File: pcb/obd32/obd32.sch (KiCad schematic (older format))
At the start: 36 parts, among them J1 USB_C_Receptacle_USB2.0, J2 Micro_SD_Card, J3 Conn_02x08_Top_Bottom, J4 USB_A, U1 LMR33630ADDA, U2 CP2102N-A01-GQFN24, U3 AP1117-33, U4 ESP32-WROOM-32, U5 SiP32431DR3, U6 MCP2562-E-MF

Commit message: Maybe version of board
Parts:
- removed C7, C8: 22µF, Capacitor_SMD:C_0805_2012Metric, symbol Device:C
- removed J1: USB_C_Receptacle_USB2.0, Connector_USB:USB_C_Receptacle_HRO_TYPE-C-31-M-12, symbol Connector:USB_C_Receptacle_USB2.0
- removed J3: Conn_02x08_Top_Bottom, Connector_PinHeader_2.54mm:PinHeader_2x08_P2.54mm_Vertical, symbol Connector_Generic:Conn_02x08_Top_Bottom
- removed J4: USB_A, Connector_USB:USB_A_Molex_105057_Vertical, symbol Connector:USB_A
- removed U1: LMR33630ADDA, Package_SO:Texas_HSOP-8-1EP_3.9x4.9mm_P1.27mm_ThermalVias, symbol Regulator_Switching:LMR33630ADDA
- removed U2: CP2102N-A01-GQFN24, Package_DFN_QFN:QFN-24-1EP_4x4mm_P0.5mm_EP2.6x2.6mm, symbol Interface_USB:CP2102N-A01-GQFN24
- added C15: 10nF, Capacitor_SMD:C_0201_0603Metric, symbol Device:C
- added C16: 0.47µF, Capacitor_SMD:C_0201_0603Metric, symbol Device:C
- added C17, C18: 0.1µF, Capacitor_SMD:C_0201_0603Metric, symbol Device:C
- added D3, D4, D5: LED, LED_SMD:LED_0402_1005Metric, symbol Device:LED
- added J1: Conn_01x04_Male, Connector_Molex:Molex_PicoBlade_53048-0410_1x04_P1.25mm_Horizontal, symbol Connector:Conn_01x04_Male
- added J3: OBD2, OBD2:OBD2, symbol OBD2:OBD2
- added J4: 67329-8040, 67329-8040:673298040, symbol 67329-8040:67329-8040
- added J5: Conn_01x04_Female, Connector_PinSocket_2.54mm:PinSocket_1x04_P2.54mm_Vertical_SMD_Pin1Left, symbol Connector:Conn_01x04_Female
- added R10, R11: 4K7, Resistor_SMD:R_0201_0603Metric, symbol Device:R
- added R12, R13: 65R, Resistor_SMD:R_0201_0603Metric, symbol Device:R
- added R14: 5R, Resistor_SMD:R_0201_0603Metric, symbol Device:R
- added SW1, SW2: SW_Push, Button_Switch_SMD:SW_SPST_B3U-3000P-B, symbol Switch:SW_Push
- added U1: LMR33630BDDA, Package_SO:Texas_HSOP-8-1EP_3.9x4.9mm_P1.27mm_ThermalVias, symbol Regulator_Switching:LMR33630BDDA
- added U2: ICM-20689, ICM-20689:QFN50P400X400X95-25N-D, symbol ICM-20689:ICM-20689
- added U7: LPS25HB, Package_LGA:ST_HLGA-10_2.5x2.5mm_P0.6mm_LayoutBorder3x2y, symbol Sensor_Pressure:LPS25HB
- C11, C12, C13, C14, C4: value 100nF -> 0.1µF; footprint Capacitor_SMD:C_0805_2012Metric -> Capacitor_SMD:C_0201_0603Metric
- C3: footprint Capacitor_SMD:C_0805_2012Metric -> Capacitor_SMD:C_0402_1005Metric
- C9: footprint Capacitor_SMD:C_0805_2012Metric -> Capacitor_SMD:C_0603_1608Metric
- L1: value 8µH -> 2.2µH; footprint Inductor_SMD:L_Coilcraft_XxL4040 -> TDK_SPM5030:TDK_SPM5030
- R1, R2, R3, R4, R7, R8, R9: footprint Resistor_SMD:R_0603_1608Metric -> Resistor_SMD:R_0201_0603Metric
- R5, R6: value 5K1 -> 100K; footprint Resistor_SMD:R_0603_1608Metric -> Resistor_SMD:R_0201_0603Metric
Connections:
- net labels added: BARO_INT, ESP32_EN, ESP32_MISC, GPS_RX, GPS_TX, I2C0_SCL, I2C0_SDA, IMU_INT, LED_B, LED_G, LED_R
- net labels removed: Earth, USB_D+, USB_D-
- wire segments 72 -> 75
- no-connect marks 0 -> 2
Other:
- moved on the sheet: C11, C12, R7, R8, U4, U5

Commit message: Board: Add USB-C and CP2102 UART converter
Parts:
- removed J1: Conn_01x04_Male, Connector_Molex:Molex_PicoBlade_53048-0410_1x04_P1.25mm_Horizontal, symbol Connector:Conn_01x04_Male
- added C7: 4.7µF, Capacitor_SMD:C_0201_0603Metric, symbol Device:C
- added C8: 0.1µF, Capacitor_SMD:C_0201_0603Metric, symbol Device:C
- added D6: SP0503BAHT, Package_TO_SOT_SMD:SOT-143, symbol Power_Protection:SP0503BAHT
- added J1: USB_C_Receptacle_USB2.0, Connector_USB:USB_C_Receptacle_HRO_TYPE-C-31-M-12, symbol Connector:USB_C_Receptacle_USB2.0
- added R15: 1K, Resistor_SMD:R_0201_0603Metric, symbol Device:R
- added R16, R17: 5.1K, Resistor_SMD:R_0201_0603Metric, symbol Device:R
- added U8: CP2102N-A01-GQFN24, Package_DFN_QFN:QFN-24-1EP_4x4mm_P0.5mm_EP2.6x2.6mm, symbol Interface_USB:CP2102N-A01-GQFN24
- C4: footprint Capacitor_SMD:C_0201_0603Metric -> Capacitor_SMD:C_0402_1005Metric
- C9: footprint Capacitor_SMD:C_0603_1608Metric -> Capacitor_SMD:C_0805_2012Metric
- U3: value AP1117-33 -> AZ1117C-3.3; footprint Package_TO_SOT_SMD:SOT-223-3_TabPin2 -> Package_TO_SOT_SMD:SOT-89-3; symbol Regulator_Linear:AP1117-33 -> Regulator_Linear:AZ1117-3.3
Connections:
- net +3V3: now also C7.1, C8.1, R15.1, U8.5 (VIO), U8.6 (VDD)
- net +5VA: now also D6.2 (K), J1.A4 (VBUS), J1.A9 (VBUS), J1.B4 (VBUS), J1.B9 (VBUS)
- net GND: now also C7.2, C8.2, D6.1 (A), J1.A1 (GND), J1.A12 (GND), J1.B1 (GND), J1.B12 (GND), J1.S1 (SHIELD), R16.1, R17.2, U8.2 (GND), U8.25 (GND)
- net UART_RX: now also U8.21 (TXD)
- net UART_TX: now also U8.20 (RXD)
- new net: J1.A5 (CC1), R16.2
- new net: J1.B5 (CC2), R17.1
- new net: R15.2, U8.9 (~RSTb)
- new net USB_D+: D6.4 (K), J1.A6 (D+), J1.B6 (D+), U8.3 (D+)
- new net USB_D-: D6.3 (K), J1.A7 (D-), J1.B7 (D-), U8.4 (D-)
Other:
- moved on the sheet: C1, C10, C2, C3, C4, C5, C6, C9, D1, D2, J4, J5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

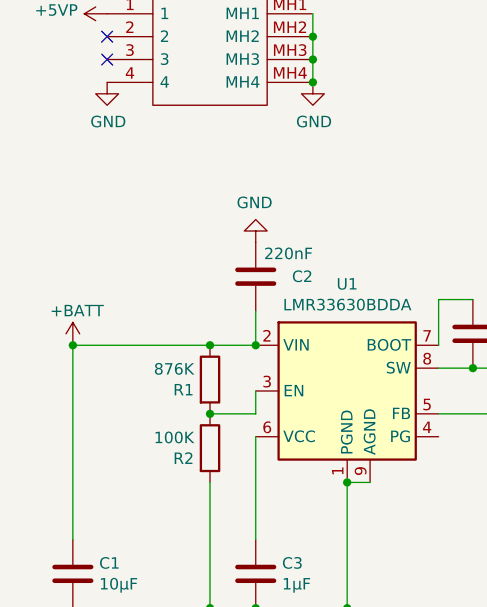
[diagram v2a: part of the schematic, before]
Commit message: Board: Add cuttable solder jumper to allow disconnection from 12V rail
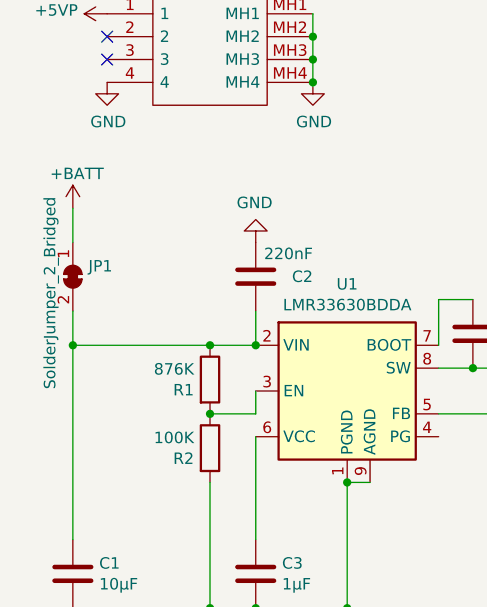
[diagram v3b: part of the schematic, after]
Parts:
- added JP1: SolderJumper_2_Bridged, Jumper:SolderJumper-2_P1.3mm_Bridged_RoundedPad1.0x1.5mm, symbol Jumper:SolderJumper_2_Bridged
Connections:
- net +BATT: now also JP1.1 (A); no longer C1.1, C2.2, R1.1, U1.2 (VIN)
- new net: C1.1, C2.2, JP1.2 (B), R1.1, U1.2 (VIN)
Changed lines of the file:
@@
 L power:+BATT #PWR0124
 U 1 1 5FC7D71E
-P 650 6400
-F 0 "#PWR0124" H 650 6250 50  0001 C CNN
-F 1 "+BATT" H 550 6550 50  0000 L CNN
-F 2 "" H 650 6400 50  0001 C CNN
-F 3 "" H 650 6400 50  0001 C CNN
-	1    650  6400
+P 650 5800
+F 0 "#PWR0124" H 650 5650 50  0001 C CNN
+F 1 "+BATT" H 550 5950 50  0000 L CNN
+F 2 "" H 650 5800 50  0001 C CNN
+F 3 "" H 650 5800 50  0001 C CNN
+	1    650  5800
 	1    0    0    -1
 $EndComp
@@
 Wire Wire Line
 	1850 7000 1950 7000
-Connection ~ 650  6400
 Wire Wire Line
 	650  6400 650  7250
@@
 	4800 6050 4900 6050
 Connection ~ 4900 6050
+$Comp
+L Jumper:SolderJumper_2_Bridged JP1
+U 1 1 5FC8024A
+P 650 6100
+F 0 "JP1" V 604 6168 50  0000 L CNN
+F 1 "SolderJumper_2_Bridged" H 300 6000 50  0000 L CNN
+F 2 "Jumper:SolderJumper-2_P1.3mm_Bridged_RoundedPad1.0x1.5mm" H 650 6100 50  0001 C CNN
+F 3 "~" H 650 6100 50  0001 C CNN
+	1    650  6100
+	0    1    1    0
+$EndComp
+Wire Wire Line
+	650  6250 650  6400
+Connection ~ 650  6400
+Wire Wire Line
+	650  5800 650  5950
 $EndSCHEMATC

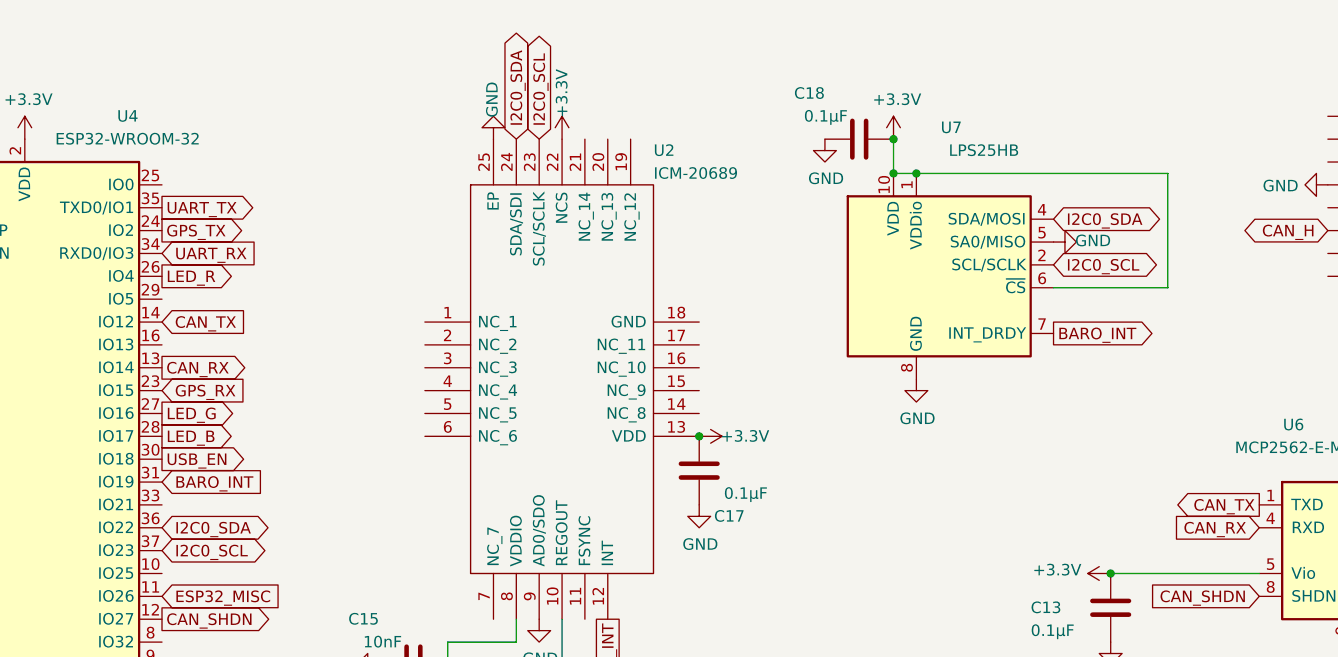
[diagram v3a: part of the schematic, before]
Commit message: Board: replace pressure sensor with more common bmp280
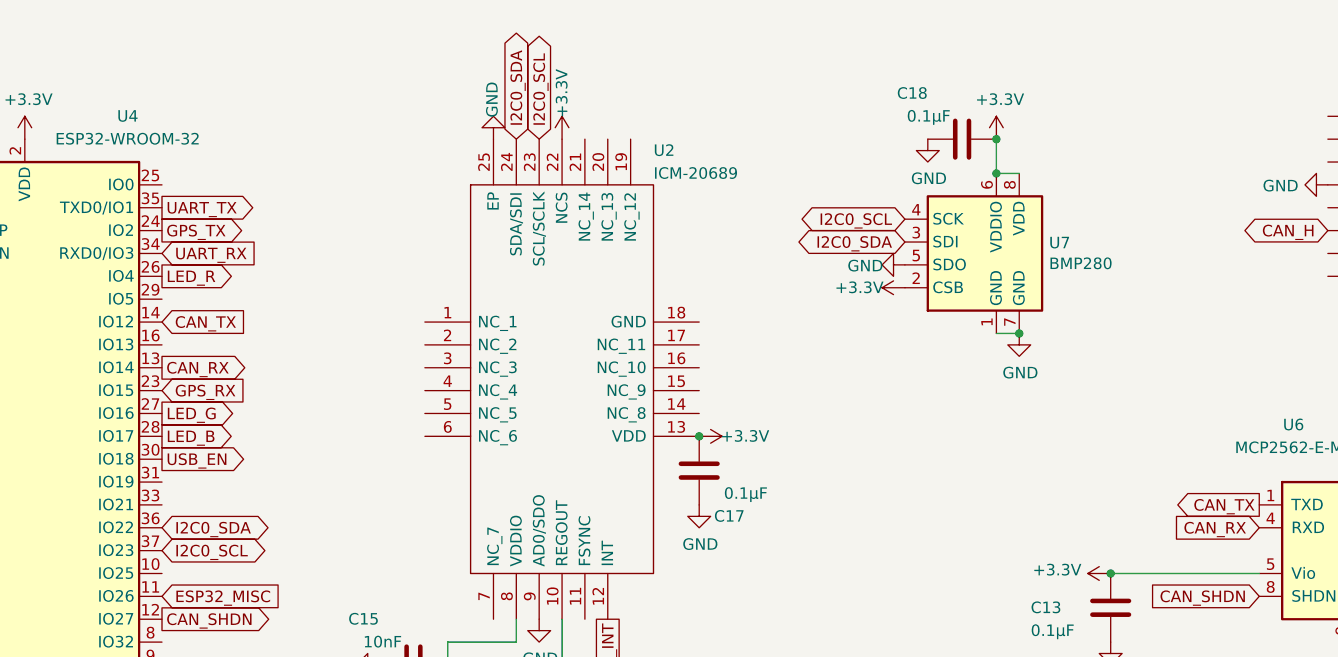
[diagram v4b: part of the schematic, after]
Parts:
- removed U7: LPS25HB, Package_LGA:ST_HLGA-10_2.5x2.5mm_P0.6mm_LayoutBorder3x2y, symbol Sensor_Pressure:LPS25HB
- added U7: BMP280, Package_LGA:Bosch_LGA-8_2x2.5mm_P0.65mm_ClockwisePinNumbering, symbol Sensor_Pressure:BMP280
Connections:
- net +3V3: now also U7.2 (CSB), U7.6 (VDDIO), U7.8 (VDD)
- net GND: now also U7.1 (GND), U7.5 (SDO), U7.7 (GND)
- net I2C0_SCL: now also U7.4 (SCK)
- net I2C0_SDA: now also U7.3 (SDI)
- net BARO_INT: no longer names the net of U4.31 (IO19)
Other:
- moved on the sheet: C18
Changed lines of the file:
@@
 	9650 6050 9650 6150
-$Comp
-L Sensor_Pressure:LPS25HB U7
-U 1 1 5FC7D0E2
-P 8050 1500
-F 0 "U7" H 8150 2100 50  0000 R CNN
-F 1 "LPS25HB" H 8400 2000 50  0000 R CNN
-F 2 "Package_LGA:ST_HLGA-10_2.5x2.5mm_P0.6mm_LayoutBorder3x2y" H 8050 1300 50  0001 C CNN
-F 3 "www.st.com/resource/en/datasheet/lps25hb.pdf" H 8100 1150 50  0001 C CNN
-	1    8050 1500
-	1    0    0    -1
-$EndComp
-Wire Wire Line
-	7950 1100 9050 1100
-Wire Wire Line
-	9050 1100 9050 1600
-Wire Wire Line
-	9050 1600 8550 1600
-$Comp
-L power:+3.3V #PWR0135
-U 1 1 5FC83F56
-P 7850 950
-F 0 "#PWR0135" H 7850 800 50  0001 C CNN
-F 1 "+3.3V" H 7865 1123 50  0000 C CNN
-F 2 "" H 7850 950 50  0001 C CNN
-F 3 "" H 7850 950 50  0001 C CNN
-	1    7850 950
-	1    0    0    -1
-$EndComp
 $Comp
 L power:+3.3V #PWR0136
@@
 L power:GND #PWR0137
 U 1 1 5FC84E03
-P 7950 2000
-F 0 "#PWR0137" H 7950 1750 50  0001 C CNN
-F 1 "GND" H 7955 1827 50  0000 C CNN
-F 2 "" H 7950 2000 50  0001 C CNN
-F 3 "" H 7950 2000 50  0001 C CNN
-	1    7950 2000
+P 8400 1800
+F 0 "#PWR0137" H 8400 1550 50  0001 C CNN
+F 1 "GND" H 8405 1627 50  0000 C CNN
+F 2 "" H 8400 1800 50  0001 C CNN
+F 3 "" H 8400 1800 50  0001 C CNN
+	1    8400 1800
 	1    0    0    -1
 $EndComp
@@
 Text GLabel 4650 2750 2    50   BiDi ~ 0
 I2C0_SCL
-Text GLabel 8550 1300 2    50   BiDi ~ 0
+Text GLabel 7900 1400 0    50   BiDi ~ 0
 I2C0_SDA
-Text GLabel 8550 1500 2    50   BiDi ~ 0
+Text GLabel 7900 1300 0    50   BiDi ~ 0
 I2C0_SCL
 Text GLabel 4650 3450 2    50   Input ~ 0
@@
 $EndComp
 Wire Wire Line
-	7950 1100 7850 1100
-Connection ~ 7950 1100
-Connection ~ 7850 1100
-$Comp
-L Device:C C18
-U 1 1 5FCF3A0C
-P 7700 950
-F 0 "C18" V 7900 1100 50  0000 L CNN
-F 1 "0.1µF" V 7800 1000 50  0000 L CNN
-F 2 "Capacitor_SMD:C_0201_0603Metric" H 7738 800 50  0001 C CNN
-F 3 "~" H 7700 950 50  0001 C CNN
-	1    7700 950
-	0    -1   -1   0
-$EndComp
-Wire Wire Line
-	7850 1100 7850 950
-Connection ~ 7850 950
-$Comp
-L power:GND #PWR0146
-U 1 1 5FCF66CC
-P 7550 950
-F 0 "#PWR0146" H 7550 700 50  0001 C CNN
-F 1 "GND" H 7555 777 50  0000 C CNN
-F 2 "" H 7550 950 50  0001 C CNN
-F 3 "" H 7550 950 50  0001 C CNN
-	1    7550 950
-	1    0    0    -1
-$EndComp
+	8400 1100 8300 1100
 $Comp
 L power:GND #PWR0147
 U 1 1 5FCF7087
-P 8550 1400
-F 0 "#PWR0147" H 8550 1150 50  0001 C CNN
-F 1 "GND" V 8555 1227 50  0000 C CNN
-F 2 "" H 8550 1400 50  0001 C CNN
-F 3 "" H 8550 1400 50  0001 C CNN
-	1    8550 1400
-	0    -1   -1   0
-$EndComp
-Text GLabel 8550 1800 2    50   Output ~ 0
-BARO_INT
-Text GLabel 4650 2450 2    50   Input ~ 0
-BARO_INT
+P 7900 1500
+F 0 "#PWR0147" H 7900 1250 50  0001 C CNN
+F 1 "GND" V 7905 1327 50  0000 C CNN
+F 2 "" H 7900 1500 50  0001 C CNN
+F 3 "" H 7900 1500 50  0001 C CNN
+	1    7900 1500
+	0    1    1    0
+$EndComp
 $Comp
 L OBD2:OBD2 J3
@@
 Wire Wire Line
 	650  5800 650  5950
+$Comp
+L Sensor_Pressure:BMP280 U7
+U 1 1 5FC9765F
+P 8300 1500
+F 0 "U7" H 8530 1596 50  0000 L CNN
+F 1 "BMP280" H 8530 1505 50  0000 L CNN
+F 2 "Package_LGA:Bosch_LGA-8_2x2.5mm_P0.65mm_ClockwisePinNumbering" H 8300 800 50  0001 C CNN
+F 3 "https://ae-bst.resource.bosch.com/media/_tech/media/datasheets/BST-BMP280-DS001.pdf" H 8300 1500 50  0001 C CNN
+	1    8300 1500
+	1    0    0    -1
+$EndComp
+Wire Wire Line
+	8300 1800 8400 1800
+Connection ~ 8400 1800
+Connection ~ 8300 1100
+$Comp
+L power:GND #PWR0146
+U 1 1 5FCF66CC
+P 8000 950
+F 0 "#PWR0146" H 8000 700 50  0001 C CNN
+F 1 "GND" H 8005 777 50  0000 C CNN
+F 2 "" H 8000 950 50  0001 C CNN
+F 3 "" H 8000 950 50  0001 C CNN
+	1    8000 950
+	1    0    0    -1
+$EndComp
+Connection ~ 8300 950
+Wire Wire Line
+	8300 1100 8300 950
+$Comp
+L Device:C C18
+U 1 1 5FCF3A0C
+P 8150 950
+F 0 "C18" V 8350 1100 50  0000 L CNN
+F 1 "0.1µF" V 8250 1000 50  0000 L CNN
+F 2 "Capacitor_SMD:C_0201_0603Metric" H 8188 800 50  0001 C CNN
+F 3 "~" H 8150 950 50  0001 C CNN
+	1    8150 950
+	0    -1   -1   0
+$EndComp
+$Comp
+L power:+3.3V #PWR0135
+U 1 1 5FC83F56
+P 8300 950
+F 0 "#PWR0135" H 8300 800 50  0001 C CNN
+F 1 "+3.3V" H 8315 1123 50  0000 C CNN
+F 2 "" H 8300 950 50  0001 C CNN
+F 3 "" H 8300 950 50  0001 C CNN
+	1    8300 950
+	1    0    0    -1
+$EndComp
+$Comp
+L power:+3.3V #PWR0159
+U 1 1 5FCB11BC
+P 7900 1600
+F 0 "#PWR0159" H 7900 1450 50  0001 C CNN
+F 1 "+3.3V" V 7900 1800 50  0000 C CNN
+F 2 "" H 7900 1600 50  0001 C CNN
+F 3 "" H 7900 1600 50  0001 C CNN
+	1    7900 1600
+	0    -1   -1   0
+$EndComp
 $EndSCHEMATC

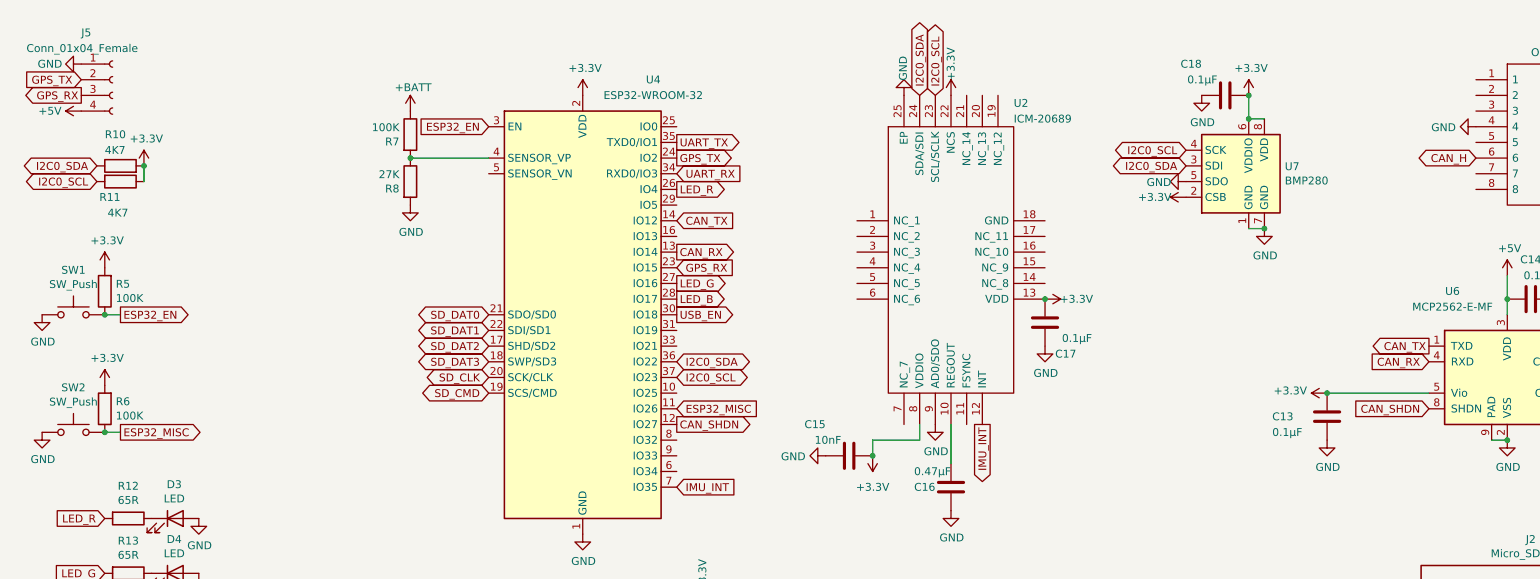
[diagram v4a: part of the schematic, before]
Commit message: Board: some refinement; Add button BOOT0
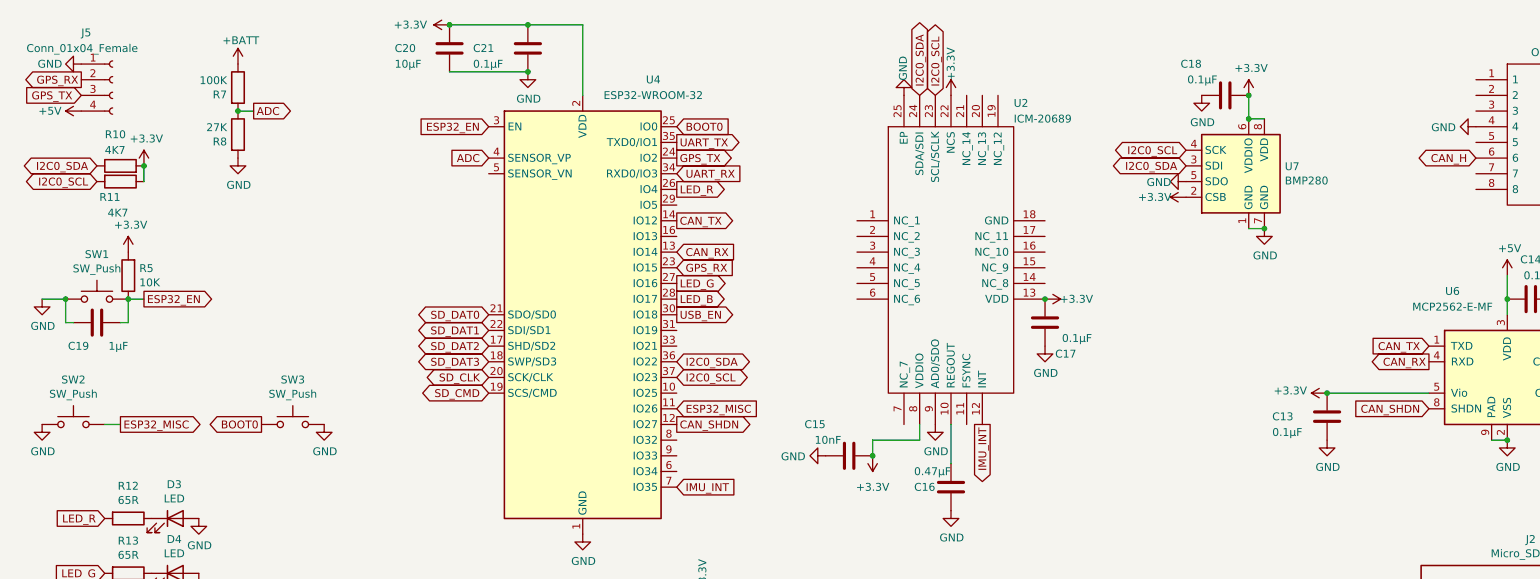
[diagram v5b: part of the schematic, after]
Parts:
- removed R6: 100K, Resistor_SMD:R_0201_0603Metric, symbol Device:R
- added C19: 1µF, Capacitor_SMD:C_0201_0603Metric, symbol Device:C
- added C20: 10µF, Capacitor_SMD:C_0805_2012Metric, symbol Device:C
- added C21: 0.1µF, Capacitor_SMD:C_0201_0603Metric, symbol Device:C
- added SW3: SW_Push, Button_Switch_SMD:SW_SPST_B3U-3000P-B, symbol Switch:SW_Push
- R5: value 100K -> 10K
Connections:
- net +3V3: now also C20.1, C21.1
- net ESP32_EN: now also C19.2
- net GND: now also C19.1, C20.2, C21.2, SW3.2
- net GPS_RX: now also J5.2 (Pin_2); no longer J5.3 (Pin_3)
- net GPS_TX: now also J5.3 (Pin_3); no longer J5.2 (Pin_2)
- net BOOT0: now reaches U4.25 (IO0)
- net BOOT0: now also SW3.1
- net ADC: now reaches R7.2, R8.1, U4.4 (SENSOR_VP)
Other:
- moved on the sheet: R5, R7, R8, SW1, SW2
